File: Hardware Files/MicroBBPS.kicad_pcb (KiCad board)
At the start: 2 copper layers, 53.3 x 30.1 mm, 29 parts, among them J2 USB_B_Micro, J5 Conn_01x02, J8 3PoleHeaderSwitch, J9 3PoleHeaderSwitch, U1 NCP1117ST50T3G, U3 NCP1117ST33T3G

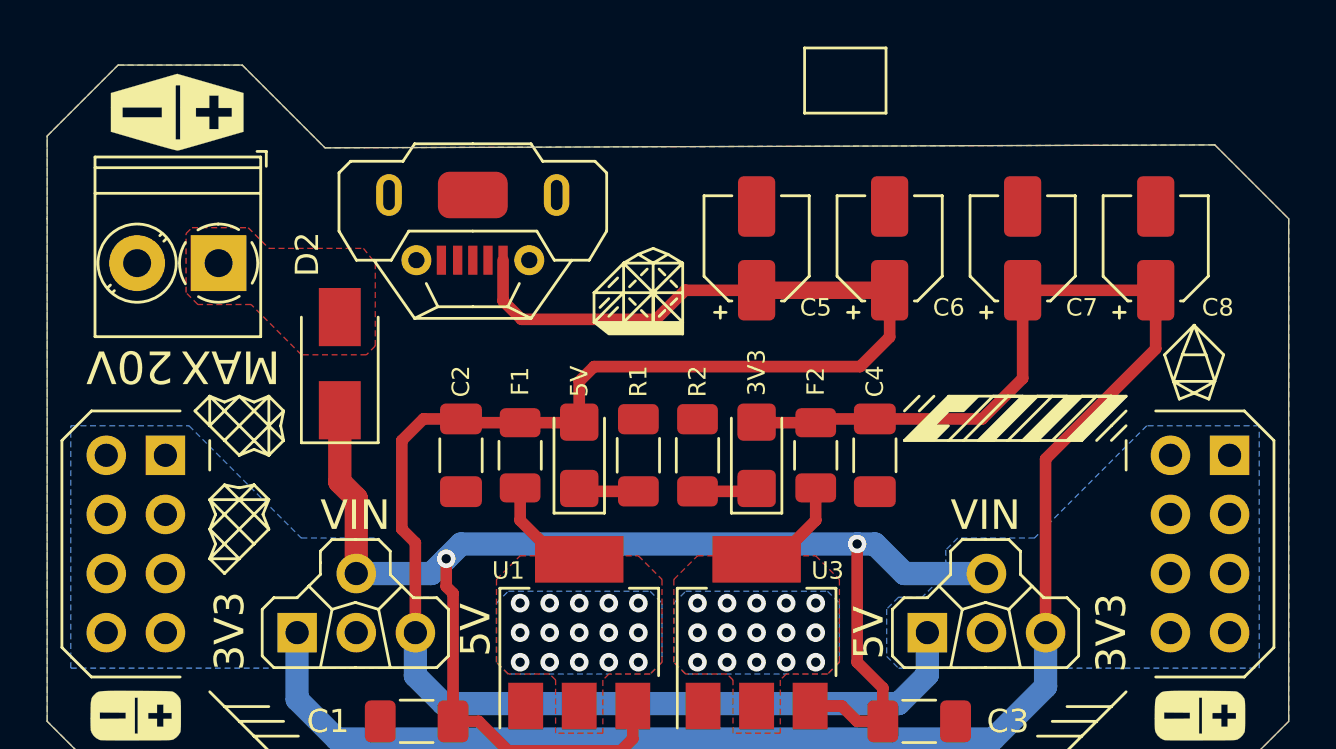
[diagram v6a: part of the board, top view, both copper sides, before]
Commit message: Finalize components Finalize placement Finalize art Finalize BoM
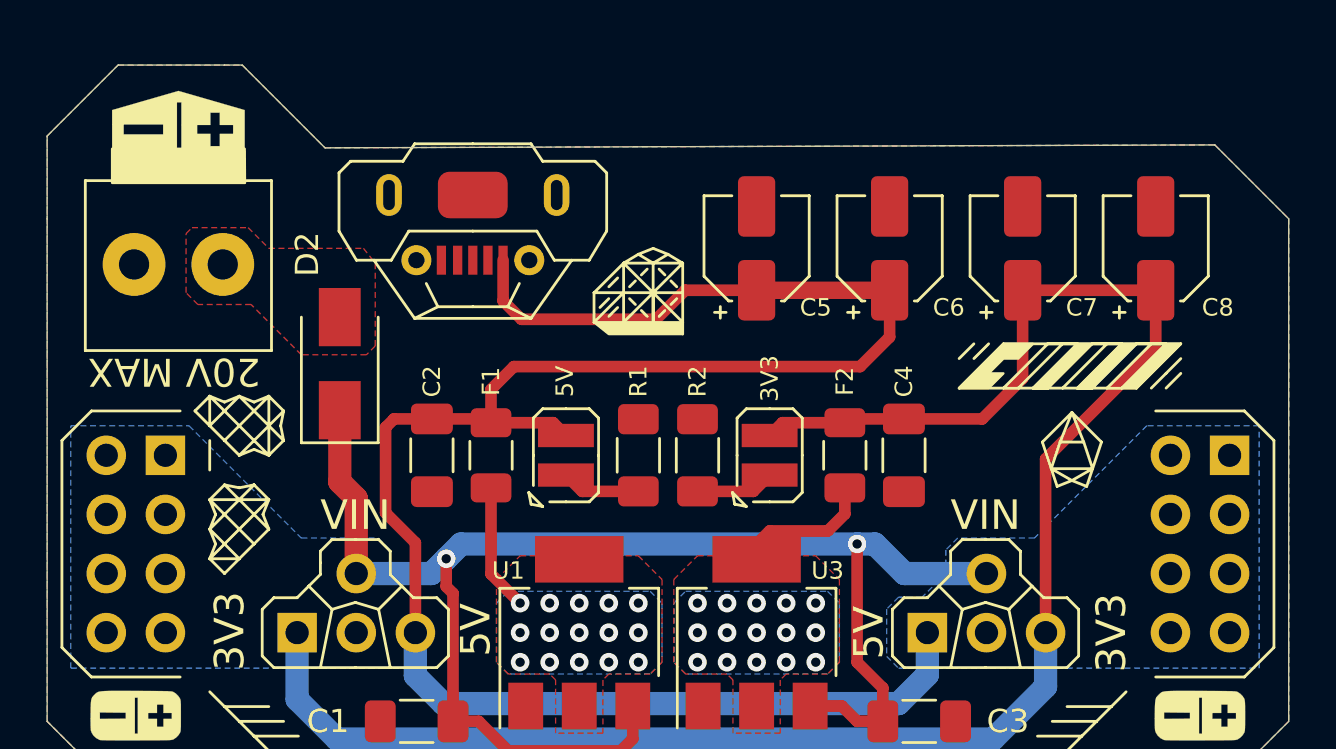
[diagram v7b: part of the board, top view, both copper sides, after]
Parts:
- D1, D3: footprint Diode_SMD:D_1206_3216Metric_Castellated -> MicroBBPS:HL-A-3528S7VC-S1-13HL
- J5: footprint TerminalBlock_Phoenix:TerminalBlock_Phoenix_PT-1,5-2-3.5-H_1x02_P3.50mm_Horizontal -> MicroBBPS:WJ124-3.81-2P
- R1: value R -> 56R 0.25W
- R2: value R -> 0R
- moved J5 1.73 mm to (3.10, -8.20)
- moved C2 1.25 mm to (14.0, 0.00)
- moved C4 1.25 mm to (34.3, 0.00)
- moved F1 1.25 mm to (16.5, 0.00)
- moved F2 1.25 mm to (31.7, 0.00)
- moved G*** 0.73 mm to (3.10, -14.0)
- moved D3 0.57 mm to (19.8, 0.00), turned to 270 degrees
- moved D1 0.56 mm to (28.5, 0.00), turned to 270 degrees
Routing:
- net +5V: track 80.3 -> 85.1 mm
- net Net-(F2-Pad2): track 4.63 -> 6.97 mm
- net Net-(F1-Pad2): track 4.63 -> 6.33 mm
- net Net-(D3-Pad1): track 2.59 -> 3.40 mm
- net Net-(D1-Pad1): track 2.59 -> 3.39 mm
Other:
- board text added: "20V MAX"
- board text removed: "20V"
- board text removed: "MAX"

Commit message: Add Gerbers & NC Drill Files
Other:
- board text added: "JLCJLCJLCJLC"
- board text added: "Order Number"
